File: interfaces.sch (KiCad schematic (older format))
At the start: 24 parts, among them J3 SI-51005-F

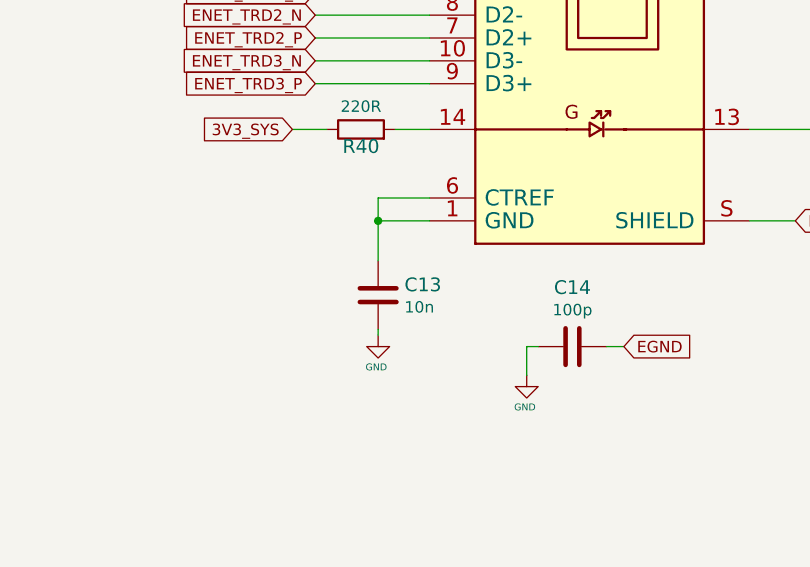
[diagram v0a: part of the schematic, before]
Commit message: Fix ethernet connector CT and GND connections
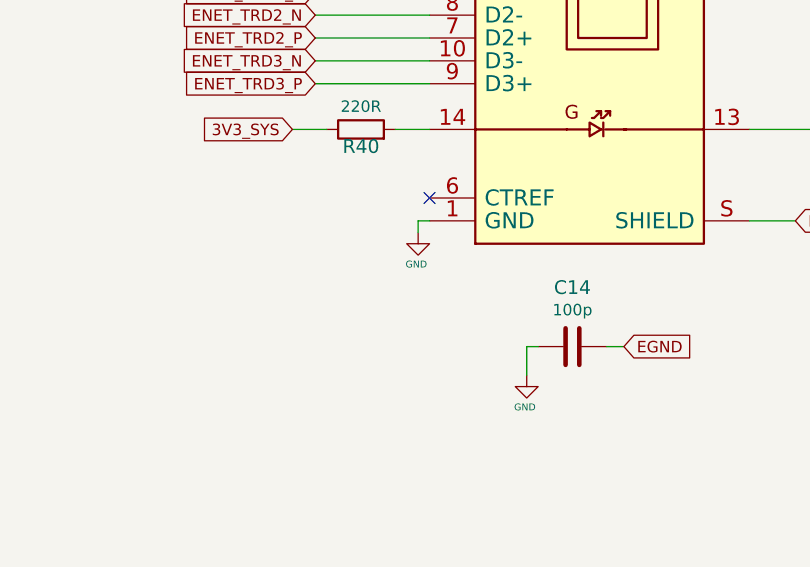
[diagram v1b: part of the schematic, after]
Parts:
- removed C13: C_10n_0402, jetson-nano-baseboard-footprints:0402-cap, symbol jetson-nano-baseboard:C_10n_0402
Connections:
- net GND: now also J3.1 (GND)
- net at J3.6 (CTREF): no longer J3.1 (GND)
- no-connect marks 18 -> 19
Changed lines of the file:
@@
 L jetson-nano-baseboard:GND #GND_036
 U 1 1 5E710455
-P 11600 7300
-F 0 "#GND_036" H 11600 7300 20  0001 C CNN
-F 1 "GND" H 11592 7160 30  0000 C CNN
-F 2 "" H 11600 7300 70  0001 C CNN
-F 3 "" H 11600 7300 70  0001 C CNN
-	1    11600 7300
+P 11775 6850
+F 0 "#GND_036" H 11775 6850 20  0001 C CNN
+F 1 "GND" H 11767 6710 30  0000 C CNN
+F 2 "" H 11775 6850 70  0001 C CNN
+F 3 "" H 11775 6850 70  0001 C CNN
+	1    11775 6850
 	1    0    0    -1
 $EndComp
@@
 	13225 6800 13425 6800
 Wire Wire Line
-	11825 6700 11600 6700
-Wire Wire Line
-	11600 6700 11600 6800
-Wire Wire Line
-	11825 6800 11600 6800
-Connection ~ 11600 6800
+	11825 6800 11775 6800
 Wire Wire Line
 	12250 7350 12250 7475
@@
 Wire Wire Line
 	12300 7350 12250 7350
-$Comp
-L jetson-nano-baseboard:C_10n_0402 C13
-U 1 1 62BF5934
-P 11600 7125
-F 0 "C13" H 11715 7170 60  0000 L CNN
-F 1 "C_10n_0402" H 11600 6975 60  0001 C CNN
-F 2 "jetson-nano-baseboard-footprints:0402-cap" H 11800 7325 60  0001 L CNN
-F 3 "" H 11600 7125 50  0001 C CNN
-F 4 "AVX" H 11800 7525 60  0001 L CNN "Manufacturer"
-F 5 "04025G103ZAT2A" H 11800 7425 60  0001 L CNN "MPN"
-F 6 "10n" H 11715 7072 50  0000 L CNN "Val"
-	1    11600 7125
-	1    0    0    -1
-$EndComp
-Wire Wire Line
-	11600 6800 11600 6975
-Wire Wire Line
-	11600 7275 11600 7300
 Wire Wire Line
 	6275 6900 8350 6900
@@
 Text GLabel 11225 5300 0    50   Input ~ 0
 3V3_SYS
+Wire Wire Line
+	11775 6800 11775 6850
+NoConn ~ 11825 6700
 $EndSCHEMATC
